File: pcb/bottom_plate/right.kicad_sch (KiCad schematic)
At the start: 22 parts

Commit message: Rework PCBs to ensure adequate clearance between them.
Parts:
- H10, H11, H12, H7, H8, H9: footprint MountingHole:MountingHole_2.2mm_M2_Pad -> MountingHole:MountingHole_2.2mm_M2; symbol Mechanical:MountingHole_Pad -> Mechanical:MountingHole
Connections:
- net GND: no longer H10.1, H11.1, H12.1, H7.1, H8.1, H9.1
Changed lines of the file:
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@@
-		)
-	)
-	(label "GND"
-		(at 259.08 210.82 270)
-		(effects
-			(font
-				(size 1.524 1.524)
-			)
-			(justify right bottom)
 		)
 	)
@@
 		)
 	)
-	(label "GND"
-		(at 259.08 185.42 270)
-		(effects
-			(font
-				(size 1.524 1.524)
-			)
-			(justify right bottom)
-		)
-	)
 	(label "MOSI"
 		(at 218.44 44.45 180)
@@
 	)
 	(label "GND"
-		(at 233.68 185.42 270)
-		(effects
-			(font
-				(size 1.524 1.524)
-			)
-			(justify right bottom)
-		)
-	)
-	(label "GND"
 		(at 64.77 88.9 270)
 		(effects
@@
 	)
 	(label "GND"
-		(at 208.28 185.42 270)
-		(effects
-			(font
-				(size 1.524 1.524)
-			)
-			(justify right bottom)
-		)
-	)
-	(label "GND"
 		(at 278.13 129.54 270)
 		(effects
@@
 		)
 	)
-	(label "GND"
-		(at 208.28 210.82 270)
-		(effects
-			(font
-				(size 1.524 1.524)
-			)
-			(justify right bottom)
-		)
-	)
 	(label "SDA"
 		(at 262.89 40.64 180)
@@
 	(label "GND"
 		(at 62.23 46.99 270)
-		(effects
-			(font
-				(size 1.524 1.524)
-			)
-			(justify right bottom)
-		)
-	)
-	(label "GND"
-		(at 233.68 210.82 270)
 		(effects
 			(font
@@
 	)
 	(symbol
-		(lib_id "Mechanical:MountingHole_Pad")
+		(lib_id "Mechanical:MountingHole")
 		(at 208.28 208.28 0)
 		(unit 1)
@@
 		(fields_autoplaced yes)
 		(property "Reference" "H8"
-			(at 210.82 205.7399 0)
+			(at 210.82 207.0099 0)
 			(show_name no)
 			(do_not_autoplace no)
@@
 		)
 		(property "Value" "MountingHole_Pad"
-			(at 210.82 208.2799 0)
-			(show_name no)
-			(do_not_autoplace no)
-			(effects
-				(font
-					(size 1.27 1.27)
-				)
-				(justify left)
-			)
-		)
-		(property "Footprint" "MountingHole:MountingHole_2.2mm_M2_Pad"
+			(at 210.82 209.5499 0)
+			(show_name no)
+			(do_not_autoplace no)
+			(effects
+				(font
+					(size 1.27 1.27)
+				)
+				(justify left)
+			)
+		)
+		(property "Footprint" "MountingHole:MountingHole_2.2mm_M2"
 			(at 208.28 208.28 0)
 			(hide yes)
@@
 			)
 		)
-		(property "Description" "Mounting Hole with connection"
+		(property "Description" "Mounting Hole without connection"
 			(at 208.28 208.28 0)
 			(hide yes)
@@
 				)
 			)
-		)
-		(pin "1"
 		)
 		(instances
@@
 	)
 	(symbol
-		(lib_id "Mechanical:MountingHole_Pad")
+		(lib_id "Mechanical:MountingHole")
 		(at 259.08 208.28 0)
 		(unit 1)
@@
 		(fields_autoplaced yes)
 		(property "Reference" "H12"
-			(at 261.62 205.7399 0)
+			(at 261.62 207.0099 0)
 			(show_name no)
 			(do_not_autoplace no)
@@
 		)
 		(property "Value" "MountingHole_Pad"
-			(at 261.62 208.2799 0)
-			(show_name no)
-			(do_not_autoplace no)
-			(effects
-				(font
-					(size 1.27 1.27)
-				)
-				(justify left)
-			)
-		)
-		(property "Footprint" "MountingHole:MountingHole_2.2mm_M2_Pad"
+			(at 261.62 209.5499 0)
+			(show_name no)
+			(do_not_autoplace no)
+			(effects
+				(font
+					(size 1.27 1.27)
+				)
+				(justify left)
+			)
+		)
+		(property "Footprint" "MountingHole:MountingHole_2.2mm_M2"
 			(at 259.08 208.28 0)
 			(hide yes)
@@
 			)
 		)
-		(property "Description" "Mounting Hole with connection"
+		(property "Description" "Mounting Hole without connection"
 			(at 259.08 208.28 0)
 			(hide yes)
@@
 				)
 			)
-		)
-		(pin "1"
 		)
 		(instances
@@
 	)
 	(symbol
-		(lib_id "Mechanical:MountingHole_Pad")
+		(lib_id "Mechanical:MountingHole")
 		(at 233.68 182.88 0)
 		(unit 1)
@@
 		(fields_autoplaced yes)
 		(property "Reference" "H9"
-			(at 236.22 180.3399 0)
+			(at 236.22 181.6099 0)
 			(show_name no)
 			(do_not_autoplace no)
@@
 		)
 		(property "Value" "MountingHole_Pad"
-			(at 236.22 182.8799 0)
-			(show_name no)
-			(do_not_autoplace no)
-			(effects
-				(font
-					(size 1.27 1.27)
-				)
-				(justify left)
-			)
-		)
-		(property "Footprint" "MountingHole:MountingHole_2.2mm_M2_Pad"
+			(at 236.22 184.1499 0)
+			(show_name no)
+			(do_not_autoplace no)
+			(effects
+				(font
+					(size 1.27 1.27)
+				)
+				(justify left)
+			)
+		)
+		(property "Footprint" "MountingHole:MountingHole_2.2mm_M2"
 			(at 233.68 182.88 0)
 			(hide yes)
@@
 			)
 		)
-		(property "Description" "Mounting Hole with connection"
+		(property "Description" "Mounting Hole without connection"
 			(at 233.68 182.88 0)
 			(hide yes)
@@
 				)
 			)
-		)
-		(pin "1"
 		)
 		(instances
@@
 	)
 	(symbol
-		(lib_id "Mechanical:MountingHole_Pad")
+		(lib_id "Mechanical:MountingHole")
 		(at 208.28 182.88 0)
 		(unit 1)
@@
 		(fields_autoplaced yes)
 		(property "Reference" "H7"
-			(at 210.82 180.3399 0)
+			(at 210.82 181.6099 0)
 			(show_name no)
 			(do_not_autoplace no)
@@
 		)
 		(property "Value" "MountingHole_Pad"
-			(at 210.82 182.8799 0)
-			(show_name no)
-			(do_not_autoplace no)
-			(effects
-				(font
-					(size 1.27 1.27)
-				)
-				(justify left)
-			)
-		)
-		(property "Footprint" "MountingHole:MountingHole_2.2mm_M2_Pad"
+			(at 210.82 184.1499 0)
+			(show_name no)
+			(do_not_autoplace no)
+			(effects
+				(font
+					(size 1.27 1.27)
+				)
+				(justify left)
+			)
+		)
+		(property "Footprint" "MountingHole:MountingHole_2.2mm_M2"
 			(at 208.28 182.88 0)
 			(hide yes)
@@
 			)
 		)
-		(property "Description" "Mounting Hole with connection"
+		(property "Description" "Mounting Hole without connection"
 			(at 208.28 182.88 0)
 			(hide yes)
@@
 				)
 			)
-		)
-		(pin "1"
 		)
 		(instances
@@
 	)
 	(symbol
-		(lib_id "Mechanical:MountingHole_Pad")
+		(lib_id "Mechanical:MountingHole")
 		(at 233.68 208.28 0)
 		(unit 1)
@@
 		(fields_autoplaced yes)
 		(property "Reference" "H10"
-			(at 236.22 205.7399 0)
+			(at 236.22 207.0099 0)
 			(show_name no)
 			(do_not_autoplace no)
@@
 		)
 		(property "Value" "MountingHole_Pad"
-			(at 236.22 208.2799 0)
-			(show_name no)
-			(do_not_autoplace no)
-			(effects
-				(font
-					(size 1.27 1.27)
-				)
-				(justify left)
-			)
-		)
-		(property "Footprint" "MountingHole:MountingHole_2.2mm_M2_Pad"
+			(at 236.22 209.5499 0)
+			(show_name no)
+			(do_not_autoplace no)
+			(effects
+				(font
+					(size 1.27 1.27)
+				)
+				(justify left)
+			)
+		)
+		(property "Footprint" "MountingHole:MountingHole_2.2mm_M2"
 			(at 233.68 208.28 0)
 			(hide yes)
@@
 			)
 		)
-		(property "Description" "Mounting Hole with connection"
+		(property "Description" "Mounting Hole without connection"
 			(at 233.68 208.28 0)
 			(hide yes)
@@
 				)
 			)
-		)
-		(pin "1"
 		)
 		(instances
@@
 	)
 	(symbol
-		(lib_id "Mechanical:MountingHole_Pad")
+		(lib_id "Mechanical:MountingHole")
 		(at 259.08 182.88 0)
 		(unit 1)
@@
 		(fields_autoplaced yes)
 		(property "Reference" "H11"
-			(at 261.62 180.3399 0)
+			(at 261.62 181.6099 0)
 			(show_name no)
 			(do_not_autoplace no)
@@
 		)
 		(property "Value" "MountingHole_Pad"
-			(at 261.62 182.8799 0)
-			(show_name no)
-			(do_not_autoplace no)
-			(effects
-				(font
-					(size 1.27 1.27)
-				)
-				(justify left)
-			)
-		)
-		(property "Footprint" "MountingHole:MountingHole_2.2mm_M2_Pad"
+			(at 261.62 184.1499 0)
+			(show_name no)
+			(do_not_autoplace no)
+			(effects
+				(font
+					(size 1.27 1.27)
+				)
+				(justify left)
+			)
+		)
+		(property "Footprint" "MountingHole:MountingHole_2.2mm_M2"
 			(at 259.08 182.88 0)
 			(hide yes)
@@
 			)
 		)
-		(property "Description" "Mounting Hole with connection"
+		(property "Description" "Mounting Hole without connection"
 			(at 259.08 182.88 0)
 			(hide yes)
@@
 			)
 		)
-		(pin "1"
-		)
 		(instances

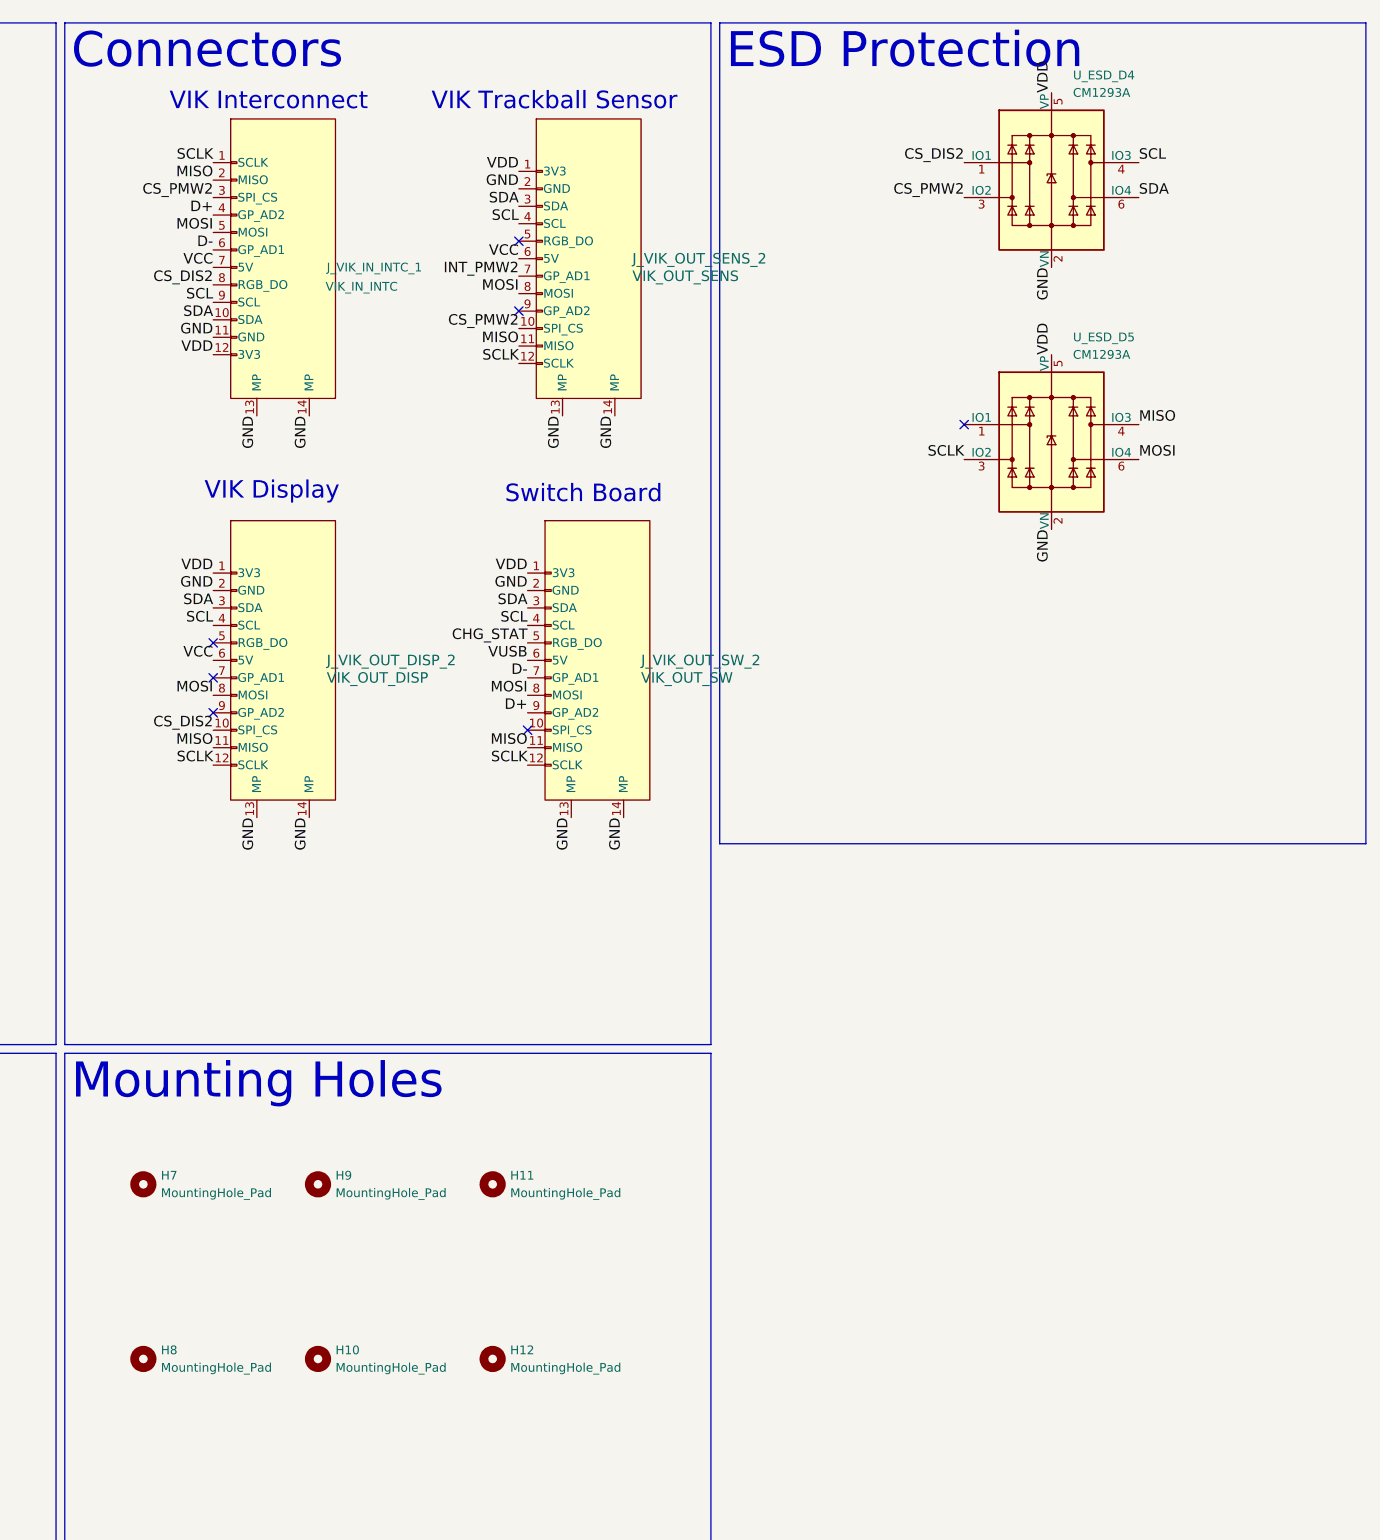
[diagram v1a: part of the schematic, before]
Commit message: Remove redundant ESD protection from bottom plate.
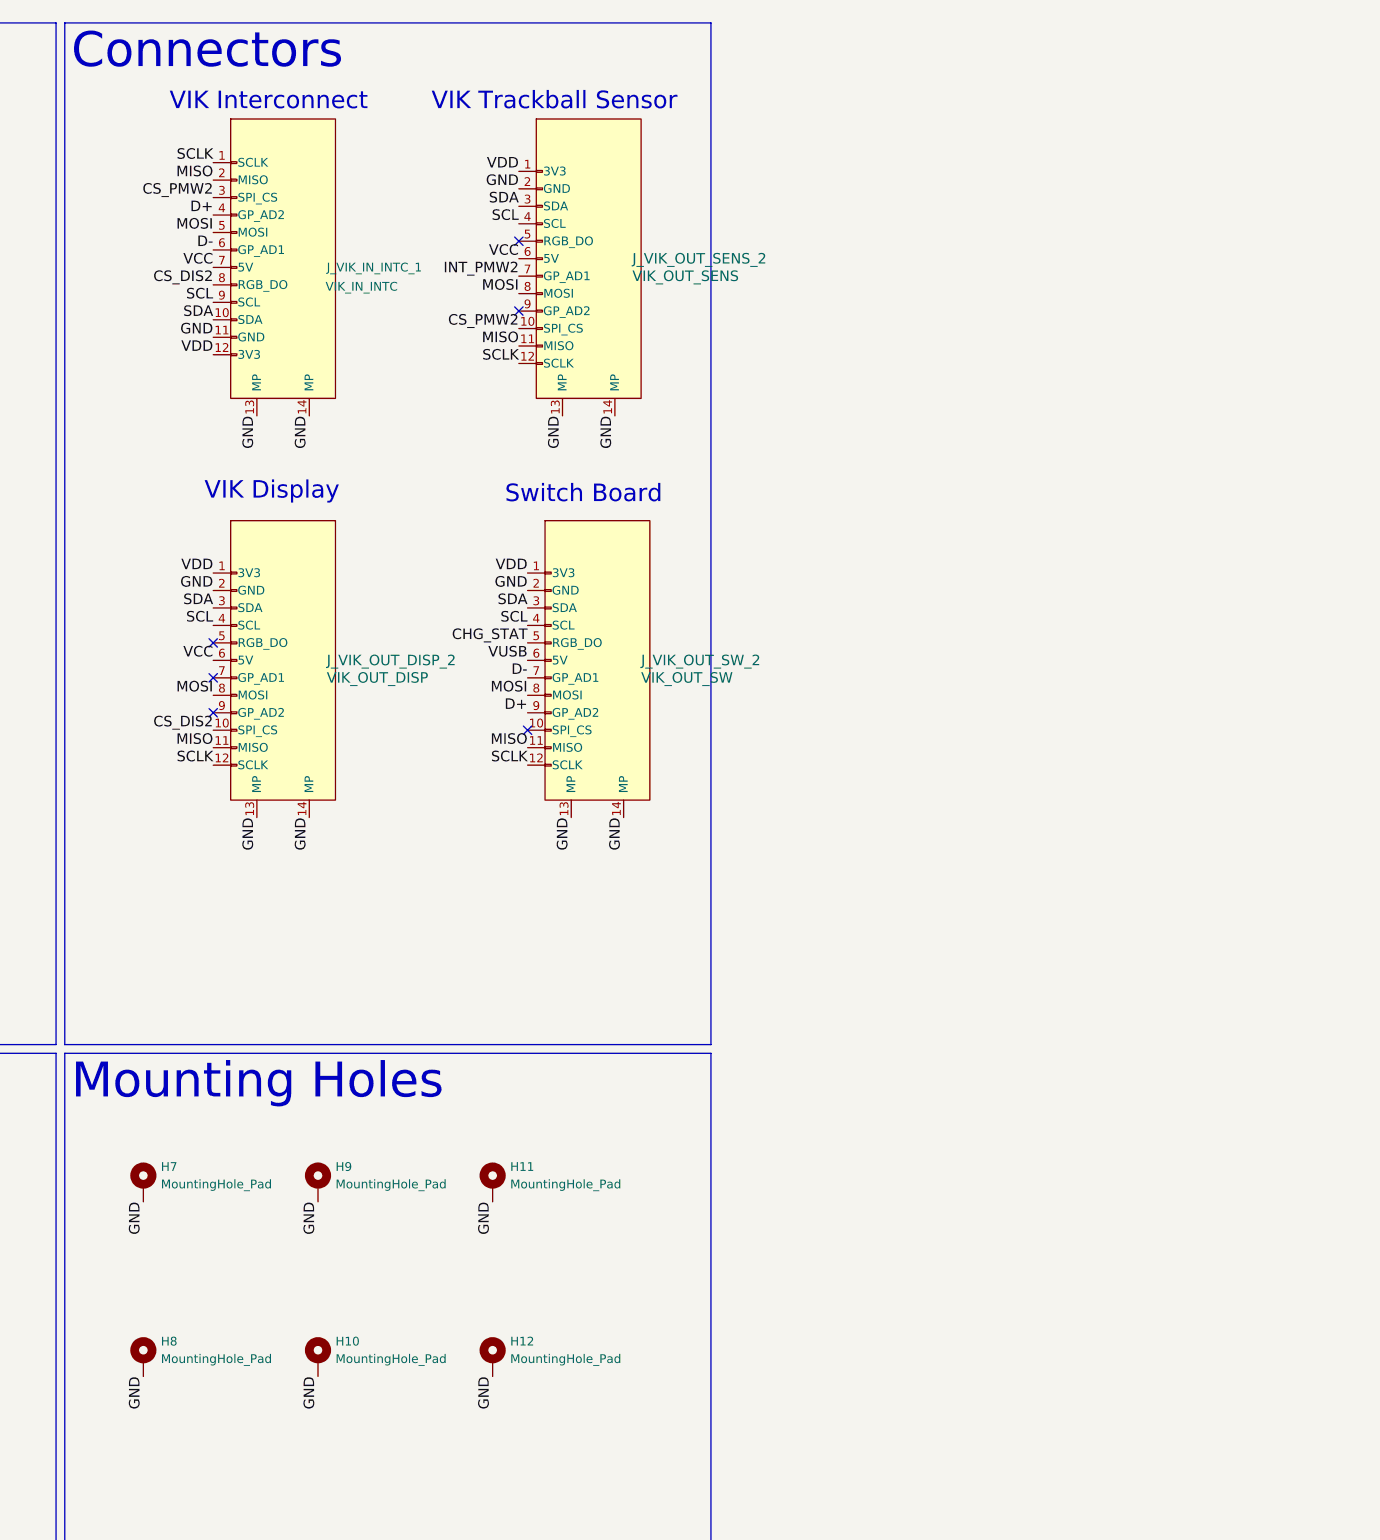
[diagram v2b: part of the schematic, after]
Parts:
- removed U_ESD_D4, U_ESD_D5: CM1293A, Package_TO_SOT_SMD:SOT-23-6, symbol Power_Protection:SRV05-4
- H10, H11, H12, H7, H8, H9: footprint MountingHole:MountingHole_2.2mm_M2 -> MountingHole:MountingHole_2.2mm_M2_Pad; symbol Mechanical:MountingHole -> Mechanical:MountingHole_Pad
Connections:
- net GND: now also H10.1, H11.1, H12.1, H7.1, H8.1, H9.1
- no-connect marks 7 -> 6

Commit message: Standardize on 0805 footprint for passive components.
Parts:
- C1, C2: footprint Capacitor_SMD:C_1206_3216Metric_Pad1.33x1.80mm_HandSolder -> Capacitor_SMD:C_0805_2012Metric_Pad1.18x1.45mm_HandSolder
- R_CHG_1, R_CHG_2, R_POW_1: footprint Resistor_SMD:R_1206_3216Metric_Pad1.30x1.75mm_HandSolder -> Resistor_SMD:R_0805_2012Metric_Pad1.20x1.40mm_HandSolder
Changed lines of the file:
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@@
 			)
 		)
-		(property "Footprint" "Capacitor_SMD:C_1206_3216Metric_Pad1.33x1.80mm_HandSolder"
+		(property "Footprint" "Capacitor_SMD:C_0805_2012Metric_Pad1.18x1.45mm_HandSolder"
 			(at 65.7352 106.68 0)
 			(hide yes)
@@
 			)
 		)
-		(property "Footprint" "Resistor_SMD:R_1206_3216Metric_Pad1.30x1.75mm_HandSolder"
+		(property "Footprint" "Resistor_SMD:R_0805_2012Metric_Pad1.20x1.40mm_HandSolder"
 			(at 111.76 105.918 90)
 			(hide yes)
@@
 			)
 		)
-		(property "Footprint" "Capacitor_SMD:C_1206_3216Metric_Pad1.33x1.80mm_HandSolder"
+		(property "Footprint" "Capacitor_SMD:C_0805_2012Metric_Pad1.18x1.45mm_HandSolder"
 			(at 65.7352 88.9 0)
 			(hide yes)
@@
 			)
 		)
-		(property "Footprint" "Resistor_SMD:R_1206_3216Metric_Pad1.30x1.75mm_HandSolder"
+		(property "Footprint" "Resistor_SMD:R_0805_2012Metric_Pad1.20x1.40mm_HandSolder"
 			(at 52.832 217.17 90)
 			(hide yes)
@@
 			)
 		)
-		(property "Footprint" "Resistor_SMD:R_1206_3216Metric_Pad1.30x1.75mm_HandSolder"
+		(property "Footprint" "Resistor_SMD:R_0805_2012Metric_Pad1.20x1.40mm_HandSolder"
 			(at 124.46 105.918 90)
 			(hide yes)

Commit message: Correct Schottky diode footprint from SOD-323 to SOD-123.
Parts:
- D_POW_1: footprint Diode_SMD:D_SOD-323 -> Diode_SMD:D_SOD-123
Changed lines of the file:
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@@
 			)
 		)
-		(property "Footprint" "Diode_SMD:D_SOD-323"
+		(property "Footprint" "Diode_SMD:D_SOD-123"
 			(at 62.23 203.835 0)
 			(hide yes)
